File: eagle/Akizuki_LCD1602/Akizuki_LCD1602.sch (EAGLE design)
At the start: 4 parts

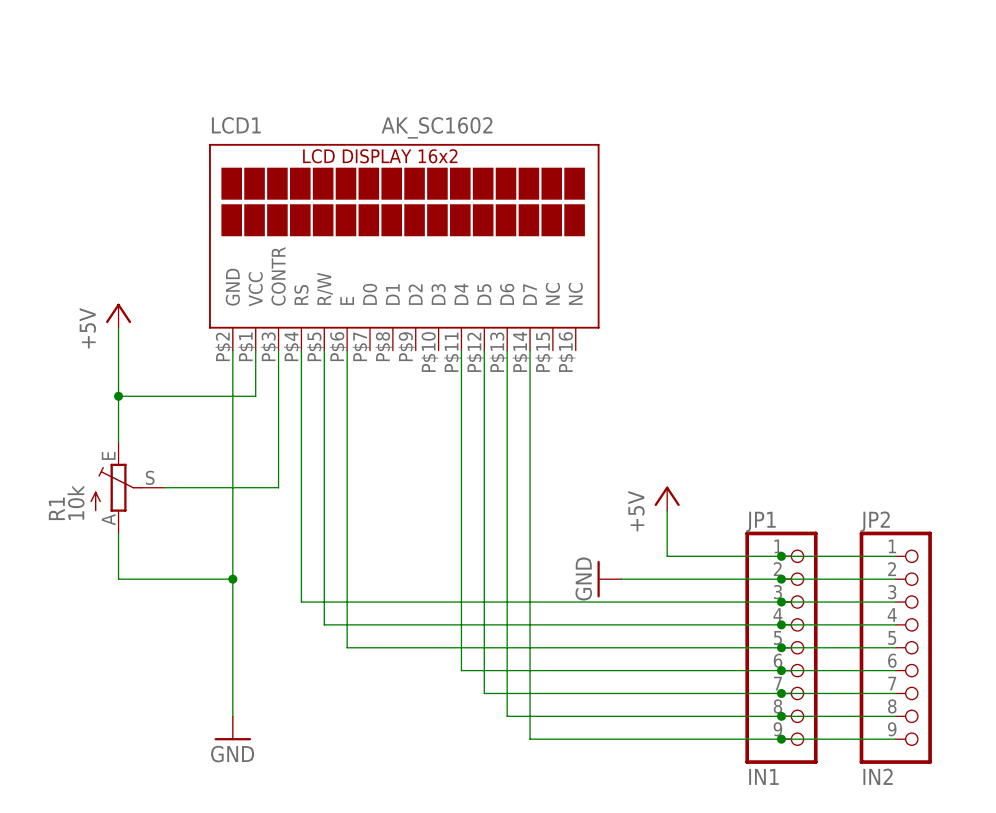
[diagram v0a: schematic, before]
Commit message: ジュンフロン線のジャンパで配線
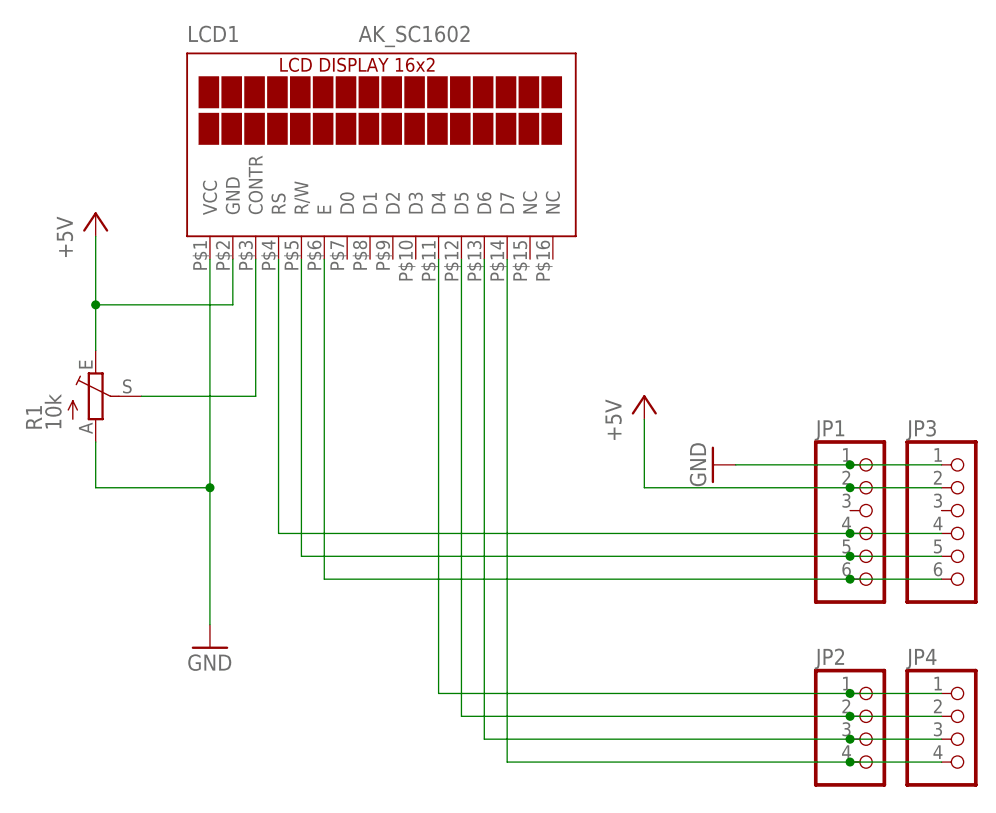
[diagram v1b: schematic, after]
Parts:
- added JP3: (no value), pinhead:PINHD-1X6
- added JP4: (no value), pinhead:PINHD-1X4
- JP1: value IN1 -> (none); device pinhead:PINHD-1X9 -> pinhead:PINHD-1X6
- JP2: value IN2 -> (none); device pinhead:PINHD-1X9 -> pinhead:PINHD-1X4
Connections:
- net +5V: now also JP1.2, JP3.2, LCD1.GND; no longer JP1.1, JP2.1, LCD1.VCC
- net GND: now also JP1.1, JP3.1, LCD1.VCC; no longer JP1.2, JP2.2, LCD1.GND
- net N$11: now also JP2.4, JP4.4; no longer JP1.9, JP2.9
- net N$2: now also JP1.4, JP3.4; no longer JP1.3, JP2.3
- net N$3: now also JP1.5, JP3.5; no longer JP1.4, JP2.4
- net N$4: now also JP1.6, JP3.6; no longer JP1.5, JP2.5
- net N$5: now also JP2.1, JP4.1; no longer JP1.6, JP2.6
- net N$6: now also JP2.2, JP4.2; no longer JP1.7, JP2.7
- net N$7: now also JP2.3, JP4.3; no longer JP1.8, JP2.8
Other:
- moved on the sheet: LCD1, R1

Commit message: Debug
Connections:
- net +5V: now also LCD1.VCC; no longer LCD1.GND
- net GND: now also LCD1.GND; no longer LCD1.VCC
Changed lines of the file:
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@@
 <instances>
 <instance part="LCD1" gate="G$1" x="119.38" y="129.54"/>
-<instance part="GND1" gate="1" x="99.06" y="71.12"/>
+<instance part="GND1" gate="1" x="101.6" y="71.12"/>
 <instance part="P+1" gate="1" x="86.36" y="119.38"/>
 <instance part="R1" gate="1" x="86.36" y="99.06"/>
@@
 <net name="GND" class="0">
 <segment>
-<pinref part="LCD1" gate="G$1" pin="VCC"/>
 <pinref part="GND1" gate="1" pin="GND"/>
-<wire x1="99.06" y1="114.3" x2="99.06" y2="88.9" width="0.1524" layer="91"/>
 <pinref part="R1" gate="1" pin="A"/>
-<wire x1="99.06" y1="88.9" x2="99.06" y2="73.66" width="0.1524" layer="91"/>
+<wire x1="101.6" y1="88.9" x2="101.6" y2="73.66" width="0.1524" layer="91"/>
 <wire x1="86.36" y1="93.98" x2="86.36" y2="88.9" width="0.1524" layer="91"/>
-<wire x1="86.36" y1="88.9" x2="99.06" y2="88.9" width="0.1524" layer="91"/>
-<junction x="99.06" y="88.9"/>
+<wire x1="86.36" y1="88.9" x2="101.6" y2="88.9" width="0.1524" layer="91"/>
+<pinref part="LCD1" gate="G$1" pin="GND"/>
+<wire x1="101.6" y1="114.3" x2="101.6" y2="88.9" width="0.1524" layer="91"/>
+<junction x="101.6" y="88.9"/>
 </segment>
 <segment>
@@
 <pinref part="P+1" gate="1" pin="+5V"/>
 <wire x1="86.36" y1="116.84" x2="86.36" y2="109.22" width="0.1524" layer="91"/>
-<wire x1="86.36" y1="109.22" x2="101.6" y2="109.22" width="0.1524" layer="91"/>
-<pinref part="LCD1" gate="G$1" pin="GND"/>
-<wire x1="101.6" y1="109.22" x2="101.6" y2="114.3" width="0.1524" layer="91"/>
+<wire x1="86.36" y1="109.22" x2="99.06" y2="109.22" width="0.1524" layer="91"/>
 <pinref part="R1" gate="1" pin="E"/>
 <wire x1="86.36" y1="104.14" x2="86.36" y2="109.22" width="0.1524" layer="91"/>
 <junction x="86.36" y="109.22"/>
+<pinref part="LCD1" gate="G$1" pin="VCC"/>
+<wire x1="99.06" y1="114.3" x2="99.06" y2="109.22" width="0.1524" layer="91"/>
 </segment>
 <segment>
